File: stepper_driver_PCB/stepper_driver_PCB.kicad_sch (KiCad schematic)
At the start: 13 parts, among them J1 POWER, J2 JTAG, J3 CTRL, J4 STEPPER, U1 STM32F411CEUx, U2 TMC2226-SA, U5 24LC512

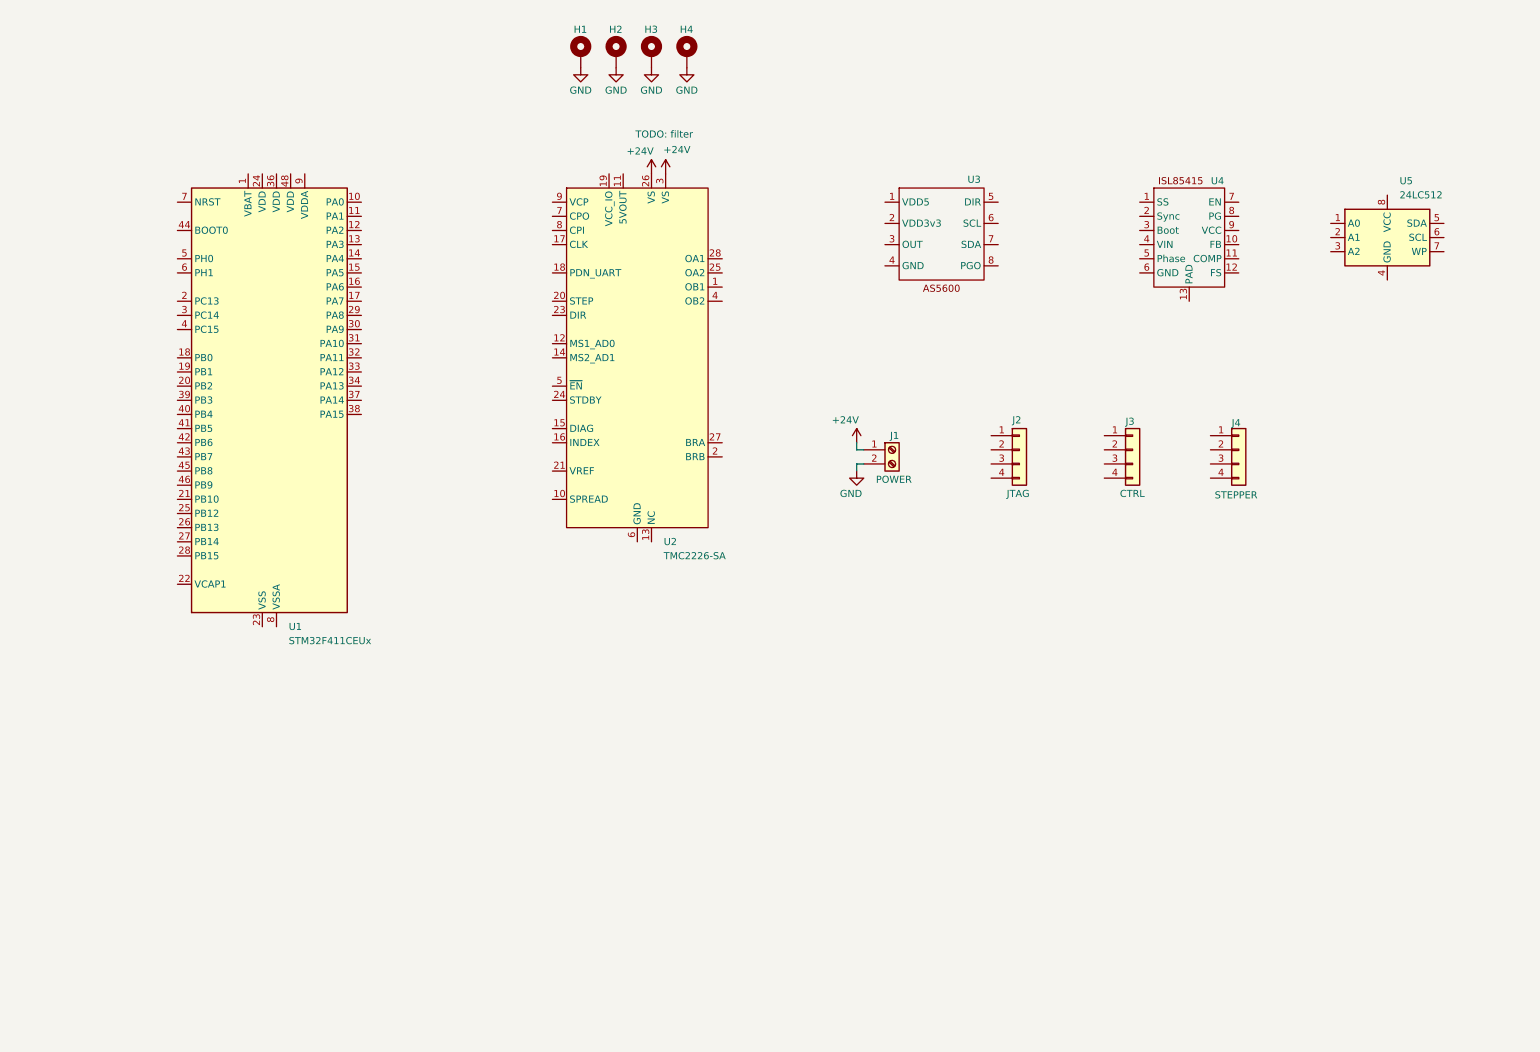
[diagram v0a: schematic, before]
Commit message: Added .gitignore and placed essential parts
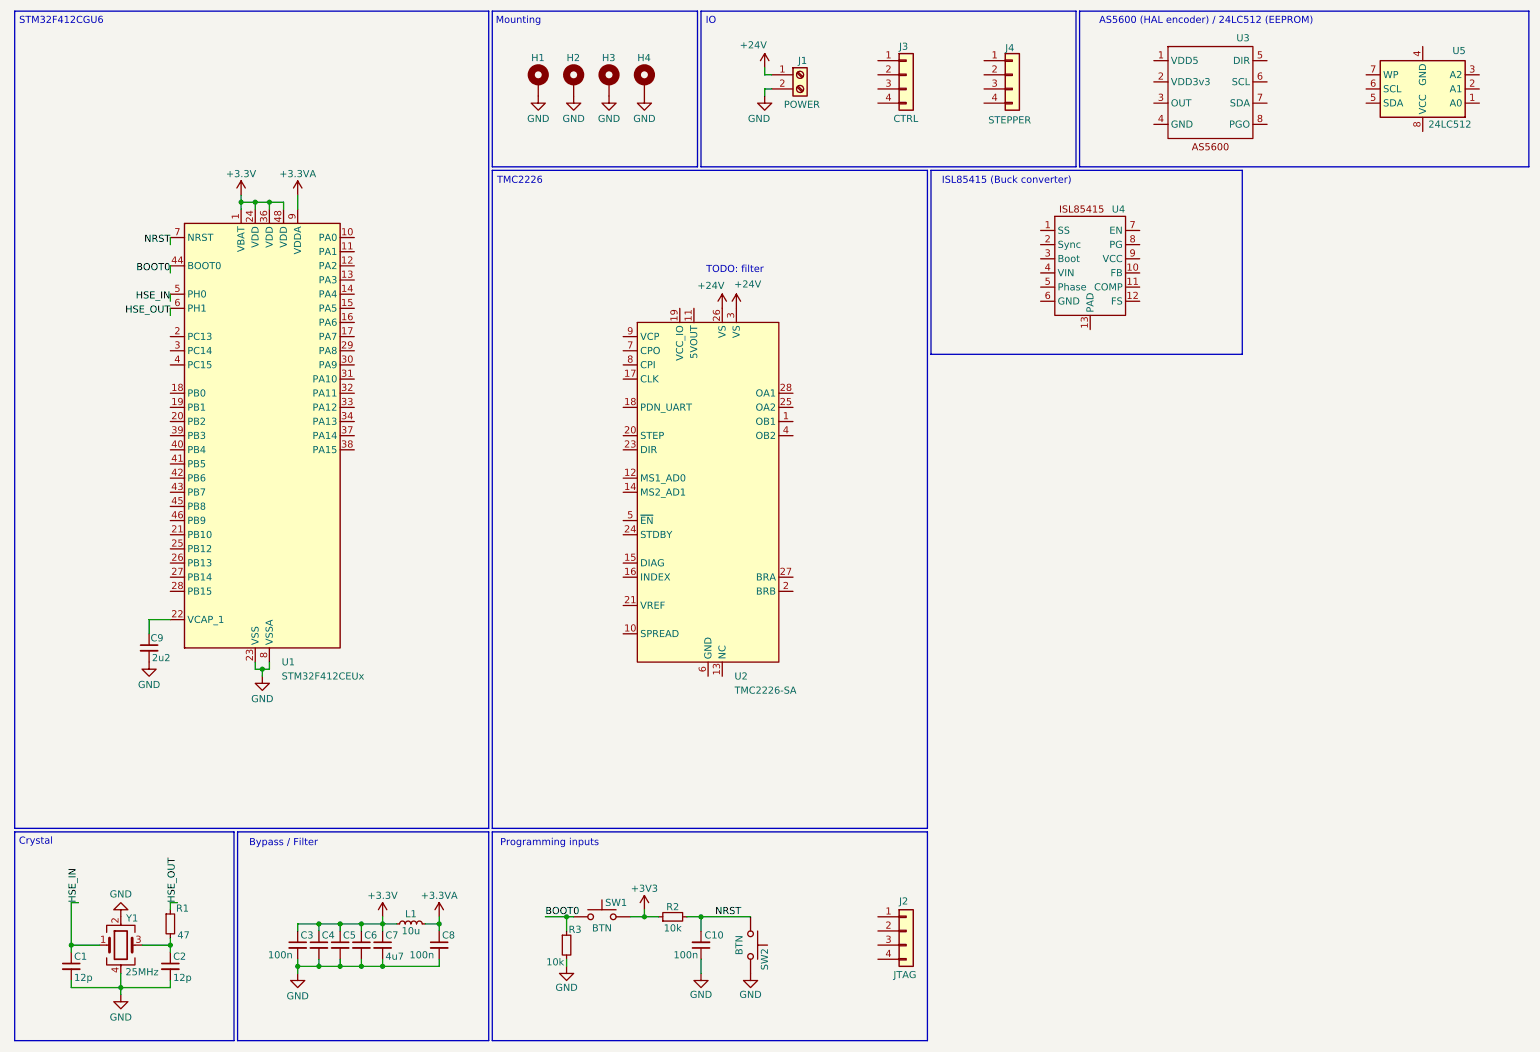
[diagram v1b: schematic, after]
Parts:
- removed U1: STM32F411CEUx, Package_DFN_QFN:QFN-48-1EP_7x7mm_P0.5mm_EP5.6x5.6mm, symbol MCU_ST_STM32F4:STM32F411CEUx
- added C1, C2: 12p, Capacitor_SMD:C_0603_1608Metric, symbol Device:C_Small
- added C10, C3, C4, C5, C6, C8: 100n, Capacitor_SMD:C_0603_1608Metric, symbol Device:C_Small
- added C7: 4u7, Capacitor_SMD:C_0603_1608Metric, symbol Device:C_Small
- added C9: 2u2, Capacitor_SMD:C_0603_1608Metric, symbol Device:C_Small
- added L1: 10u, Inductor_SMD:L_0805_2012Metric, symbol Device:L_Small
- added R1: 47, Resistor_SMD:R_0603_1608Metric, symbol Device:R_Small
- added R2, R3: 10k, Resistor_SMD:R_0603_1608Metric, symbol Device:R_Small
- added SW1, SW2: BTN, Button_Switch_SMD:SW_SPST_PTS810, symbol Switch:SW_Push
- added U1: STM32F412CEUx, Package_DFN_QFN:QFN-48-1EP_7x7mm_P0.5mm_EP5.6x5.6mm, symbol MCU_ST_STM32F4:STM32F412CEUx
- added Y1: 25MHz, Crystal:Crystal_SMD_3225-4Pin_3.2x2.5mm, symbol Device:Crystal_GND24
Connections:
- net GND: now also C1.2, C10.1, C2.2, C3.2, C4.2, C5.2, C6.2, C7.2, C8.2, C9.2, R3.2, SW2.2, U1.23 (VSS), U1.35 (VSS), U1.47 (VSS), U1.49 (VSS), U1.8 (VSSA), Y1.2, Y1.4
- new net: C2.1, R1.2, Y1.3
- new net: C9.1, U1.22 (VCAP_1)
- new net +3.3V: C3.1, C4.1, C5.1, C6.1, C7.1, L1.1, U1.1 (VBAT), U1.24 (VDD), U1.36 (VDD), U1.48 (VDD)
- new net +3.3VA: C8.1, L1.2, U1.9 (VDDA)
- new net +3V3: R2.1, SW1.2
- new net BOOT0: R3.1, SW1.1, U1.44 (BOOT0)
- new net HSE_IN: C1.1, U1.5 (PH0), Y1.1
- new net HSE_OUT: R1.1, U1.6 (PH1)
- new net NRST: C10.2, R2.2, SW2.1, U1.7 (NRST)
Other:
- note added: "AS5600 (HAL encoder) / 24LC512 (EEPROM)"
- note added: "Bypass / Filter"
- note added: "Crystal"
- note added: "IO"
- note added: "ISL85415 (Buck converter)"
- note added: "Mounting"
- note added: "Programming inputs"
- note added: "STM32F412CGU6"
- note added: "TMC2226"
- moved on the sheet: H1, H2, H3, H4, J1, J2, J3, J4, U2, U3, U4, U5

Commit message: Added USB port for configuration and testing
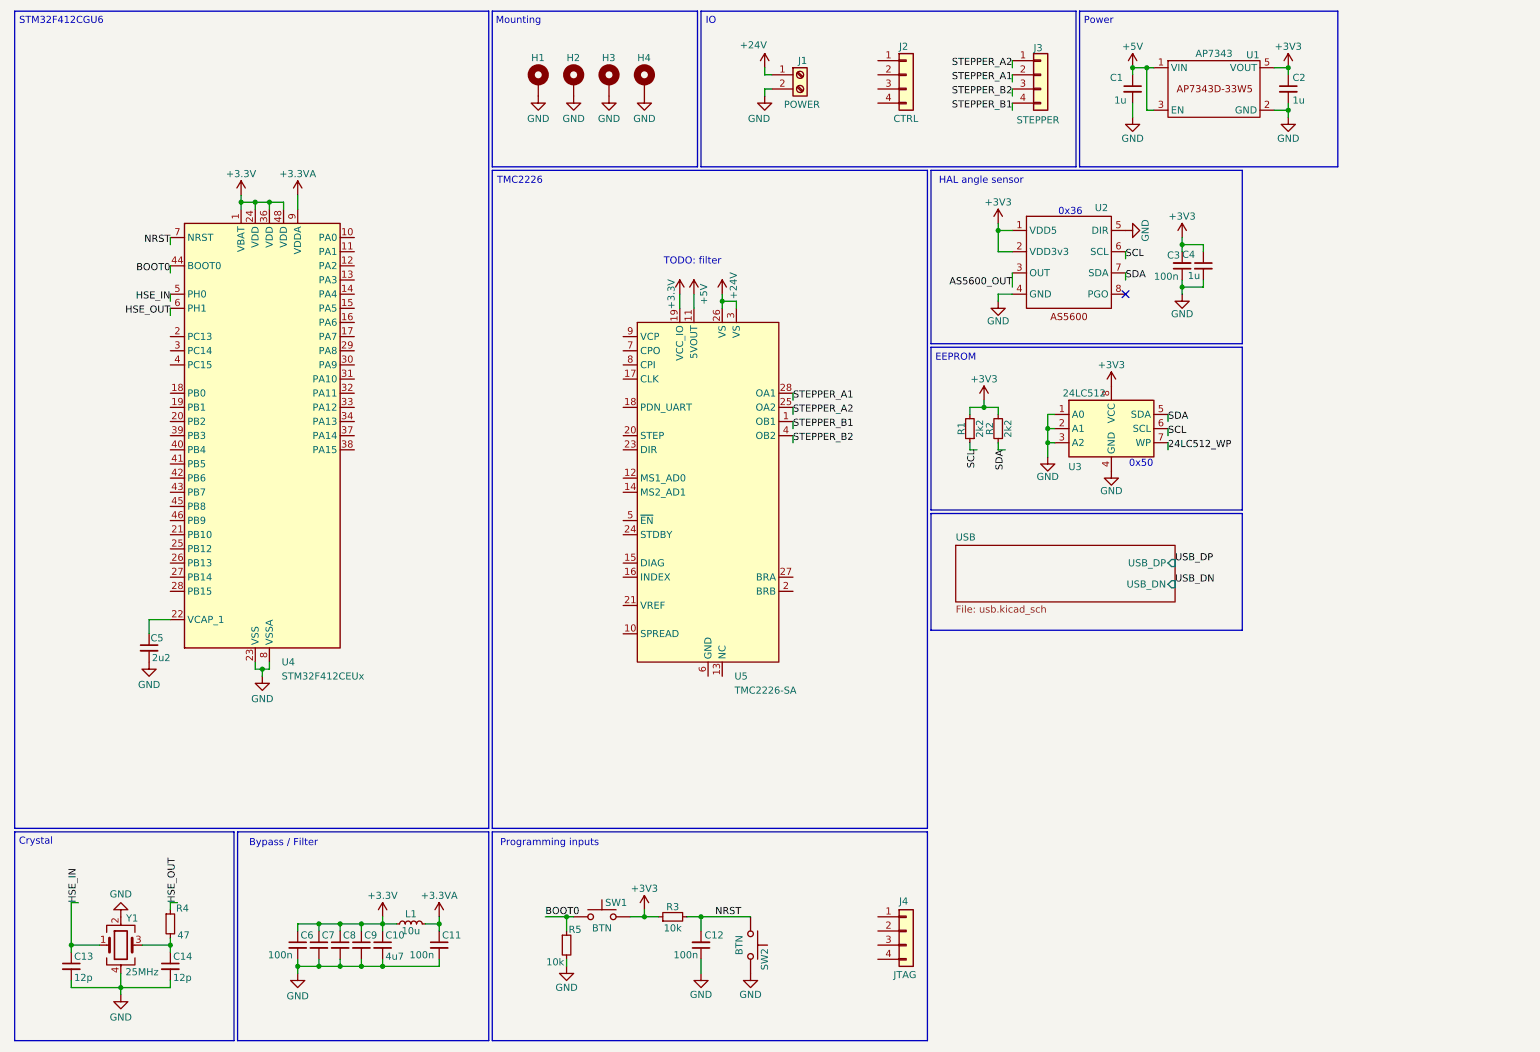
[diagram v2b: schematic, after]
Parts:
- removed U3: ~, Package_SO:SOIC-8_3.9x4.9mm_P1.27mm, symbol Marijn:AS5600
- removed U4: ~, Package_DFN_QFN:DFN-12-1EP_3x4mm_P0.5mm_EP1.7x3.3mm, symbol Marijn:ISL85415
- added C1, C2, C4: 1u, Capacitor_SMD:C_0603_1608Metric, symbol Device:C_Small
- added C3: 100n, Capacitor_SMD:C_0603_1608Metric, symbol Device:C_Small
- added R1, R2: 2k2, Resistor_SMD:R_0603_1608Metric, symbol Device:R_Small
- added U1: AP7343, Custom:SOT-25, symbol Marijn:AP7343
- added U2: ~, Package_SO:SOIC-8_3.9x4.9mm_P1.27mm, symbol Marijn:AS5600
- renumbered C7 to C10, C8 to C11, C10 to C12, C1 to C13, C2 to C14, C9 to C5, C3 to C6, C4 to C7, C5 to C8, C6 to C9, J3 to J2, J4 to J3, J2 to J4, R2 to R3, R1 to R4, R3 to R5, U5 to U3, U1 to U4, U2 to U5
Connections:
- net +3.3V: now also U5.19 (VCC_IO)
- net +3V3: now also U3.8 (VCC), C2.1, C3.2, C4.1, R1.2, R2.2, U1.5 (VOUT), U2.1 (VDD5), U2.2 (VDD3v3)
- net GND: now also U3.1 (A0), U3.2 (A1), U3.3 (A2), U3.4 (GND), C1.2, C2.2, C3.1, C4.2, U1.2 (GND), U2.4 (GND), U2.5 (DIR)
- net STEPPER_B1: now reaches U5.1 (OB1)
- net STEPPER_B1: now also J3.4 (Pin_4)
- net +5V: now reaches U5.11 (5VOUT)
- net +5V: now also C1.1, U1.1 (VIN), U1.3 (EN)
- net STEPPER_A2: now reaches U5.25 (OA2)
- net STEPPER_A2: now also J3.1 (Pin_1)
- net STEPPER_A1: now reaches U5.28 (OA1)
- net STEPPER_A1: now also J3.2 (Pin_2)
- net STEPPER_B2: now reaches U5.4 (OB2)
- net STEPPER_B2: now also J3.3 (Pin_3)
- net SDA: now reaches U3.5 (SDA)
- net SDA: now also R2.1, U2.7 (SDA)
- net SCL: now reaches U3.6 (SCL)
- net SCL: now also R1.1, U2.6 (SCL)
- net 24LC512_WP: now reaches U3.7 (WP)
- new net AS5600_OUT: U2.3 (OUT)
- no-connect marks 0 -> 1
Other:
- added sheet USB (usb.kicad_sch)
- note added: "0x36"
- note added: "0x50"
- note added: "EEPROM"
- note added: "HAL angle sensor"
- note added: "Power"
- note removed: "AS5600 (HAL encoder) / 24LC512 (EEPROM)"
- note removed: "ISL85415 (Buck converter)"
- moved on the sheet: J3, U3

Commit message: Layout
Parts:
- added C15: 22n/50v, Capacitor_SMD:C_0603_1608Metric, symbol Device:C_Small
- added C16: 100n/50v, Capacitor_SMD:C_0603_1608Metric, symbol Device:C_Small
- added D1: PWR, LED_SMD:LED_0603_1608Metric, symbol Device:LED
- added D2: STATUS, LED_SMD:LED_0603_1608Metric, symbol Device:LED
- added R10, R9: 2k2, Resistor_SMD:R_0603_1608Metric, symbol Device:R_Small
- added R7: 5k1, Resistor_SMD:R_0603_1608Metric, symbol Device:R_Small
- added R8: 1k, Resistor_SMD:R_0603_1608Metric, symbol Device:R_Small
- C5: value 2u2 -> 4u7
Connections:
- net +24V: now also C16.1
- net +3.3V: now also R10.2; no longer C10.1, C6.1, C7.1, C8.1, C9.1, L1.1, U4.1 (VBAT), U4.24 (VDD), U4.36 (VDD), U4.48 (VDD), U5.19 (VCC_IO)
- net +3.3VA: now also U5.21 (VREF)
- net +3V3: now also C10.1, C6.1, C7.1, C8.1, C9.1, J4.1 (Pin_1), L1.1, U4.1 (VBAT), U4.24 (VDD), U4.36 (VDD), U4.48 (VDD), U5.19 (VCC_IO), R7.1, R8.1, R9.2
- net 24LC512_WP: now also U4.38 (PA15), R9.1
- net AS5600_OUT: now also U4.10 (PA0)
- net GND: now also J4.4 (Pin_4), U5.17 (CLK), U5.2 (BRB), U5.22 (GND), U5.27 (BRA), U5.29 (GND), U5.6 (GND), D1.1 (K)
- net SCL: no longer U2.6 (SCL), U3.6 (SCL)
- net SDA: no longer U2.7 (SDA), U3.5 (SDA)
- net USB_DN: now also U4.32 (PA11)
- net USB_DP: now also U4.33 (PA12)
- net TMC_SPREAD: now reaches U5.10 (SPREAD)
- net TMC_SPREAD: now also U4.40 (PB4)
- net TMC_MS1: now reaches U5.12 (MS1_AD0)
- net TMC_MS1: now also U4.20 (PB2)
- net TMC_MS2: now reaches U5.14 (MS2_AD1)
- net TMC_MS2: now also U4.39 (PB3)
- net TMC_DIAG: now reaches U5.15 (DIAG)
- net TMC_DIAG: now also U4.43 (PB7)
- net TMC_NDP/UART: now reaches U5.18 (PDN_UART)
- net TMC_NDP/UART: now also U4.42 (PB6)
- net TMC_STEP: now reaches U5.20 (STEP)
- net TMC_STEP: now also U4.18 (PB0)
- net TMC_DIR: now reaches U5.23 (DIR)
- net TMC_DIR: now also U4.19 (PB1)
- net TMC_STDBY: now reaches U5.24 (STDBY)
- net TMC_STDBY: now also U4.41 (PB5)
- net TMC_NEN: now reaches U5.5 (~{EN})
- net TMC_NEN: now also U4.45 (PB8), R10.1
- net at U5.7 (CPO): now also C15.1
- net at U5.8 (CPI): now also C15.2
- net at U5.9 (VCP): now also C16.2
- net JTAG_SWCLK: now reaches J4.2 (Pin_2)
- net JTAG_SWCLK: now also U4.37 (PA14)
- net JTAG_SWDIO: now reaches J4.3 (Pin_3)
- net JTAG_SWDIO: now also U4.34 (PA13)
- net SPI_NCS: now reaches J2.1 (Pin_1)
- net SPI_NCS: now also U4.14 (PA4)
- net SPI_CLK: now reaches J2.2 (Pin_2)
- net SPI_CLK: now also U4.15 (PA5)
- net SPI_MISO: now reaches J2.3 (Pin_3)
- net SPI_MISO: now also U4.16 (PA6)
- net SPI_MOSI: now reaches J2.4 (Pin_4)
- net SPI_MOSI: now also U4.17 (PA7)
- net I2C_SDA: now reaches U4.21 (PB10)
- net I2C_SDA: now also U2.7 (SDA), U3.5 (SDA)
- net STATUS: now reaches U4.31 (PA10)
- net STATUS: now also D2.1 (K)
- net I2C_SCL: now reaches U4.46 (PB9)
- net I2C_SCL: now also U2.6 (SCL), U3.6 (SCL)
- new net: D2.2 (A), R8.2
- new net: D1.2 (A), R7.2
- no-connect marks 1 -> 15
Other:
- note added: "<1ohm?"
- note added: "Analog PWM"
- note added: "CTRL"
- note added: "DIAG: HI on stall, reset by NEN HI INDEX: Pulse every 4 steps"
- note added: "Driver CTRL"
- note added: "I2C"
- note added: "LED"
- note added: "Programming and Settings"
- note added: "Stepper"
- note added: "Stepper Driver"
- note added: "USB"
- moved on the sheet: C3, C4, J2, U2

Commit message: Layout V2
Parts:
- removed R2, R9: 2k2, Resistor_SMD:R_0603_1608Metric, symbol Device:R_Small
- removed U3: 24LC512, Package_DIP:DIP-8_W7.62mm_Socket, symbol Memory_EEPROM:24LC512
- added U7: W25Q128JVS, Package_SO:SOIC-8_5.23x5.23mm_P1.27mm, symbol Memory_Flash:W25Q128JVS
- R1: value 2k2 -> 1k
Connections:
- net +3.3V is gone; now on net +3V3: R10.2
- net SCL is gone; now on net TMC_UART_TX: R1.1
- net +3V3: now also U7.8 (VCC); no longer R1.2
- net GND: now also U7.4 (GND)
- net JTAG_SWCLK: now also J4.3 (Pin_3); no longer J4.2 (Pin_2)
- net JTAG_SWDIO: now also J4.2 (Pin_2); no longer J4.3 (Pin_3)
- net STATUS: now also U4.29 (PA8); no longer U4.31 (PA10)
- net STEPPER_A1: now also J3.3 (Pin_3); no longer J3.2 (Pin_2)
- net STEPPER_A2: now also J3.4 (Pin_4); no longer J3.1 (Pin_1)
- net STEPPER_B1: now also J3.2 (Pin_2); no longer J3.4 (Pin_4)
- net STEPPER_B2: now also J3.1 (Pin_1); no longer J3.3 (Pin_3)
- net TMC_DIAG: now also U4.18 (PB0); no longer U4.43 (PB7)
- net TMC_DIR: now also U4.26 (PB13); no longer U4.19 (PB1)
- net TMC_MS1: now also U4.11 (PA1); no longer U4.20 (PB2)
- net TMC_MS2: now also U4.12 (PA2); no longer U4.39 (PB3)
- net TMC_NEN: now also U4.13 (PA3); no longer U4.45 (PB8)
- net TMC_SPREAD: now also U4.27 (PB14); no longer U4.40 (PB4)
- net TMC_STDBY: now also U4.28 (PB15); no longer U4.41 (PB5)
- net TMC_STEP: now also U4.25 (PB12); no longer U4.18 (PB0)
- net TMC_INDEX: now reaches U5.16 (INDEX)
- net TMC_INDEX: now also U4.19 (PB1)
- net TMC_UART_TX: now reaches U4.30 (PA9)
- net 24LC512_WP renamed FLASH_SPI_NCS
- net FLASH_SPI_NCS: now also U7.1 (~{CS})
- net SPI_CLK renamed CTRL_SPI_CLK
- net CTRL_SPI_CLK: now also J2.3 (Pin_3); no longer J2.2 (Pin_2)
- net SPI_MISO renamed CTRL_SPI_MISO
- net CTRL_SPI_MISO: now also J2.2 (Pin_2); no longer J2.3 (Pin_3)
- net SPI_MOSI renamed CTRL_SPI_MOSI
- net CTRL_SPI_MOSI: now also J2.1 (Pin_1); no longer J2.4 (Pin_4)
- net SPI_NCS renamed CTRL_SPI_NCS
- net CTRL_SPI_NCS: now also J2.4 (Pin_4); no longer J2.1 (Pin_1)
- net TMC_NDP/UART renamed TMC_UART_RX
- net TMC_UART_RX: now also R1.2, U4.31 (PA10); no longer U4.42 (PB6)
- new net FLASH_SPI_CLK: U4.39 (PB3), U7.6 (CLK)
- new net FLASH_SPI_MISO: U4.40 (PB4), U7.2 (DO(IO1))
- new net FLASH_SPI_MOSI: U4.41 (PB5), U7.5 (DI(IO0))
- new net W25Q128_NRST: U4.43 (PB7), U7.7 (IO3)
- new net W25Q128_NWP: U4.42 (PB6), U7.3 (IO2)
- no-connect marks 15 -> 6
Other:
- note added: "(HARD)"
- note added: "(MASTER)"
- note added: "(SLAVE)"
- note added: "(SOFT)"
- note added: "(settings) TMC"
- note added: "FLASH"
- note added: "HSE"
- note added: "SPI flash (W25Q128)"
- note added: "STATUS"
- note added: "TMC"
- note added: "TMC (INT)"
- note added: "TMC (actions)"
- note removed: "0x50"
- note removed: "EEPROM"
- moved on the sheet: C15, J2
